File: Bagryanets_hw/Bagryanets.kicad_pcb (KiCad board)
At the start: 2 copper layers, 45 x 80 mm, 82 parts, among them Q1 SI2302CDS, Q2 SI2302CDS, Q3 SI2302CDS, U1 MCP1700-3302E_SOT23, U2 LMV721M5, U3 LMV721M5, X1 USBC-16P, X2 PLS-6 LOCK, X3 HU-2/WF-2 Battery, X4 HU-2/WF-2 SPST Switch

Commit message: Updated schematic
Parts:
- added C38: 680p, Capacitors:CAP_0603, F.Cu at (80.1, 182.1)
- added C39: 680p, Capacitors:CAP_0603, F.Cu at (80.1, 184.1)
- added C40: 100n, Capacitors:CAP_0603, F.Cu at (63.3, 125.7)
- added R15: 1k, Resistors:RES_0603, F.Cu at (76.5, 182.4)
- added R16: 1k, Resistors:RES_0603, F.Cu at (76.5, 185.2)
- C1, C10, C12, C13, C14, C16, C17, C19, C2, C21, C23, C24, C25, C3, C8: footprint Capacitors:CAP_0402 -> Capacitors:CAP_0603
- C5, C6: value * -> 1p*
- H1, H2, H3, H4: value MountingHole -> M3 MountingHole
- HA1: value HCM1201X -> HC0901A
- X3, X4: footprint Connector_PinHeader_2.54mm:PinHeader_1x02_P2.54mm_Vertical -> Connector_PinHeader_2.54mm:PinHeader_1x02_P2.54mm_Horizontal
- moved DD2 101.3 mm to (143.0, 121.0)
- moved H1 95.5 mm to (127.0, 131.0)
- moved H2 95.5 mm to (157.0, 95.0)
- moved H3 95.5 mm to (127.0, 95.0)
- moved H4 95.5 mm to (157.0, 131.0)
- moved C17 92.7 mm to (100.9, 87.2)
- moved C15 92.6 mm to (103.0, 87.2)
- moved C29 92.6 mm to (95.8, 75.3)
- moved C3 92.6 mm to (88.7, 181.2)
- moved C31 92.6 mm to (100.6, 75.6)
- moved C35 92.6 mm to (129.2, 76.8)
- moved C36 92.6 mm to (127.6, 77.3)
- moved C4 92.6 mm to (63.8, 161.9)
- moved DA1 92.6 mm to (129.7, 78.8)
- moved DD1 92.6 mm to (103.0, 82.4)
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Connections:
- C5 pad 1: /IR_IN1 -> Net-(C5-Pad1)
- C6 pad 1: /IR_IN2 -> Net-(C6-Pad1)
- DD2 pad 14: /IR_IN1 -> /L.RESET
- DD2 pad 15: /IR_IN2 -> /IR_IN1
- DD2 pad 16: /UART_TX -> /IR_IN2
- DD2 pad 17: /UART_RX -> unconnected-(DD2-PA3-Pad17)
- DD2 pad 2: unconnected-(DD2-Pad2) -> /L.DIO1
- DD2 pad 25: unconnected-(DD2-Pad25) -> /L.DIO0
- DD2 pad 26: /IR_O -> unconnected-(DD2-PB0-Pad26)
- DD2 pad 27: unconnected-(DD2-Pad27) -> /Buzzer
- DD2 pad 37: unconnected-(DD2-Pad37) -> /LED.B
- DD2 pad 38: unconnected-(DD2-Pad38) -> /LED.R
- DD2 pad 39: unconnected-(DD2-Pad39) -> /LED.G
- DD2 pad 41: /L.RESET -> /IR_Out
- DD2 pad 42: unconnected-(DD2-Pad42) -> /UART_TX
- DD2 pad 43: unconnected-(DD2-Pad43) -> /UART_RX
- DD2 pad 55: /Buzzer -> unconnected-(DD2-PB3-Pad55)
- DD2 pad 56: /LED.B -> unconnected-(DD2-PB4-Pad56)
- DD2 pad 57: /LED.R -> unconnected-(DD2-PB5-Pad57)
- DD2 pad 58: /LED.G -> unconnected-(DD2-PB6-Pad58)
- DD2 pad 7: unconnected-(DD2-Pad7) -> Net-(DD2-NRST)
- DD2 pad 8: /L.DIO0 -> unconnected-(DD2-PC0-Pad8)
- DD2 pad 9: /L.DIO1 -> unconnected-(DD2-PC1-Pad9)
- Q2 pad 1: /IR_O -> /IR_Out
- R6 pad 2: /IR_IN1 -> Net-(C5-Pad1)
- R7 pad 2: /IR_IN2 -> Net-(C6-Pad1)
- U2 pad 1: /IR_IN1 -> Net-(C5-Pad1)
- U3 pad 1: /IR_IN2 -> Net-(C6-Pad1)
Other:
- board size 45 x 80 mm -> 45 x 88 mm

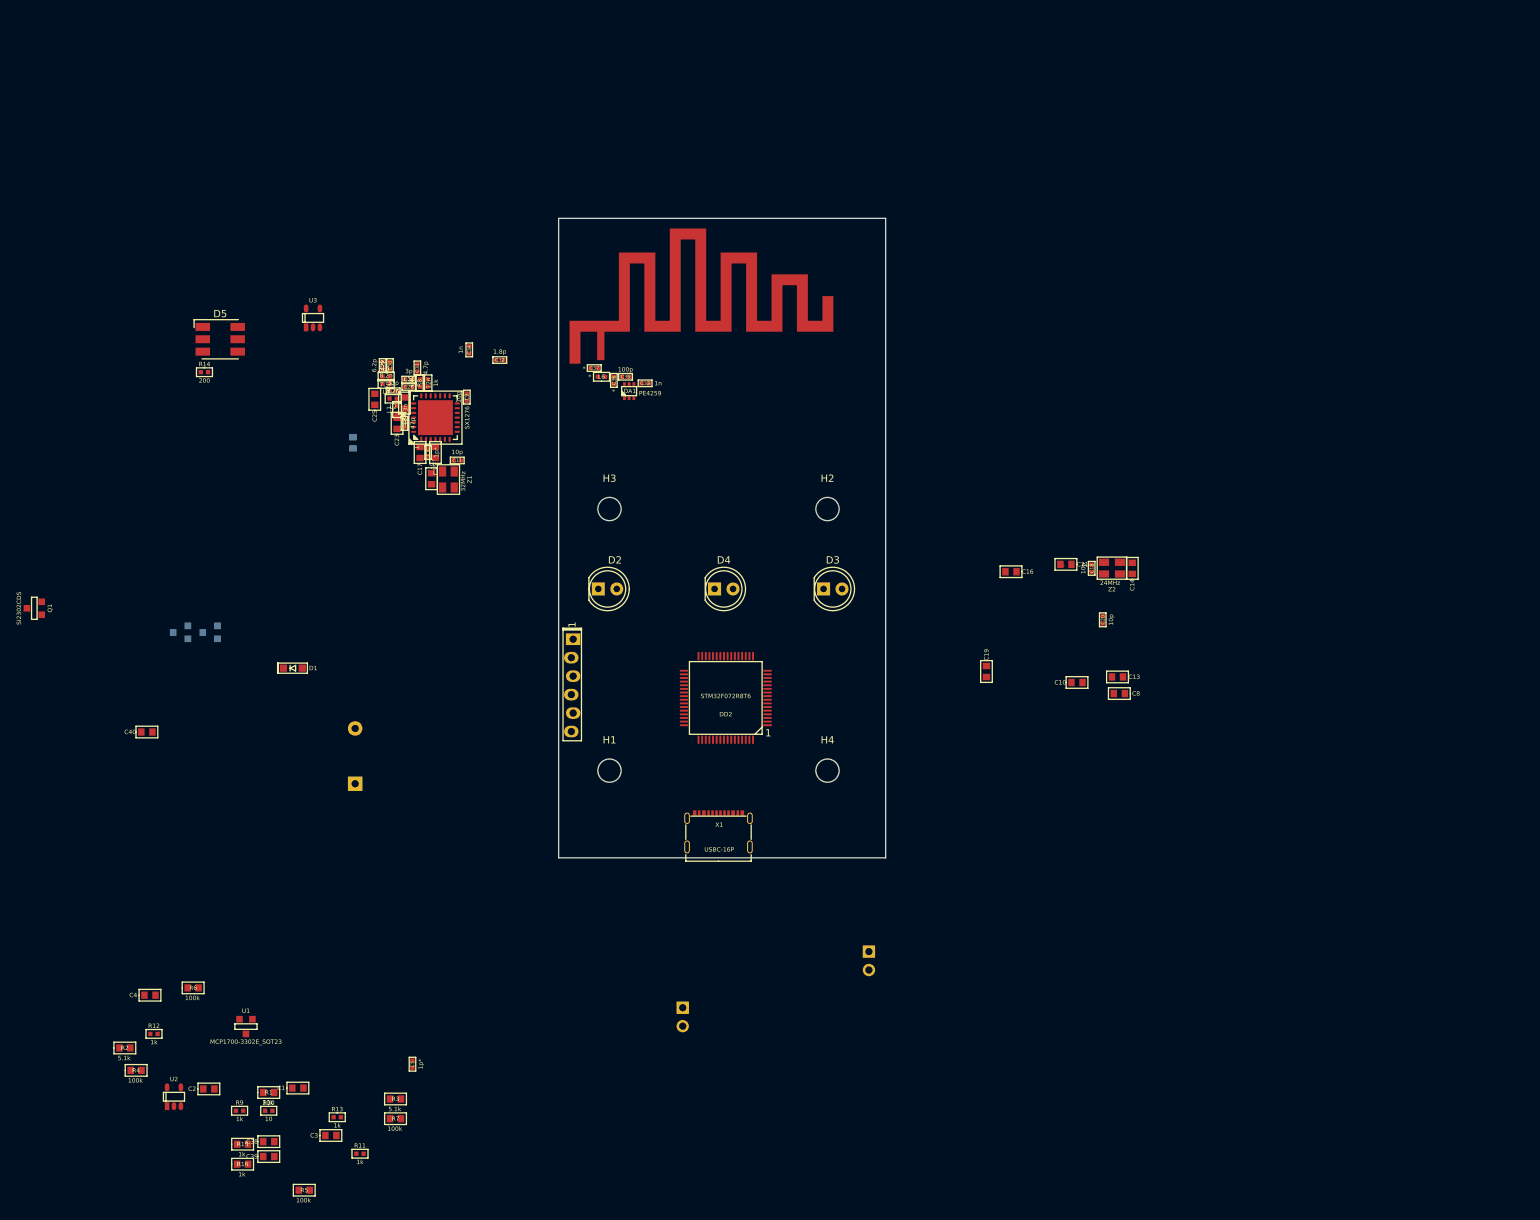
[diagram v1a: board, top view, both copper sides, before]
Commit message: PCB wiring, updated casing
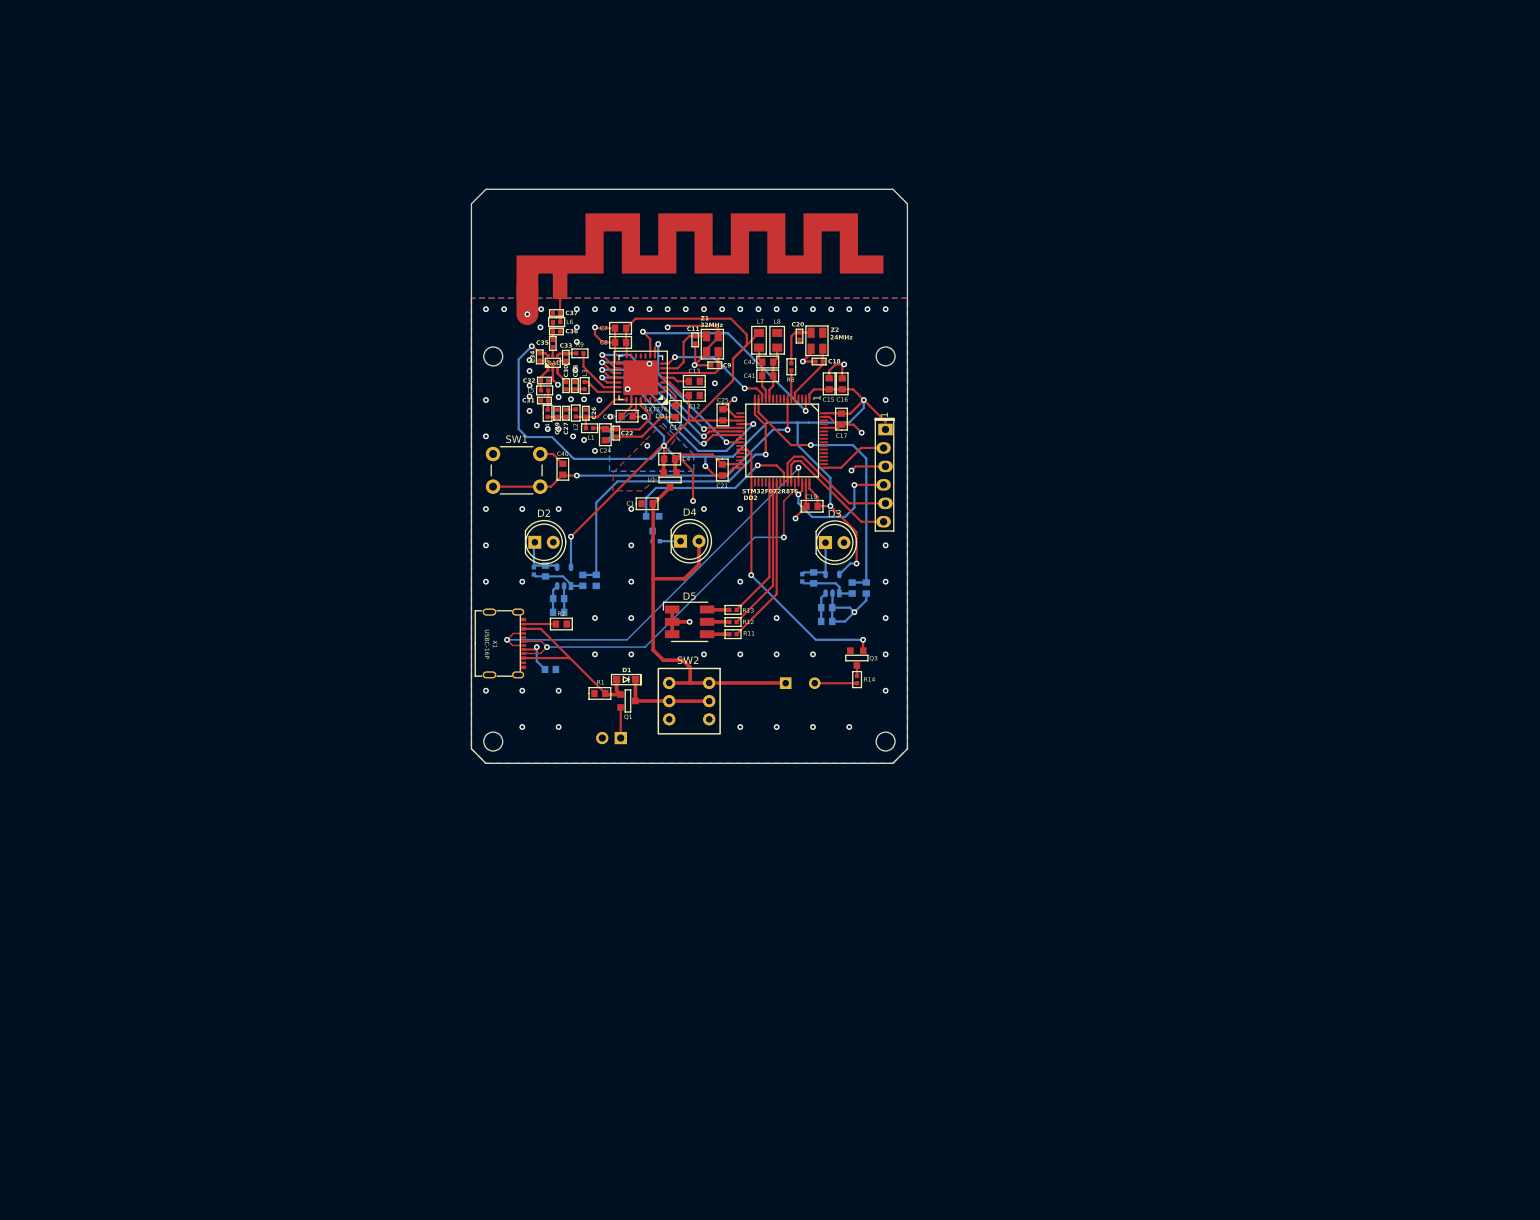
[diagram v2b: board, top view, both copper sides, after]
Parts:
- removed C23: 10n, Capacitors:CAP_0603
- removed H1, H2, H3, H4: M3 MountingHole, MountingHole:MountingHole_3.2mm_M3
- removed X4: HU-2/WF-2 SPST Switch, Connector_PinHeader_2.54mm:PinHeader_1x02_P2.54mm_Horizontal
- added ANT1: ANT_GENERAL, Kais_Lib:Antenna_868_Bagryanets, F.Cu at (120.2, 66.1)
- added C41: 10n, Capacitors:CAP_0603, F.Cu at (148.8, 76.7)
- added C42: 10u, Capacitors:CAP_0603, F.Cu at (148.8, 74.8)
- added L7: 10uH, Inductors:IND_0805, F.Cu at (147.6, 71.8)
- added L8: 10uH, Inductors:IND_0805, F.Cu at (150.1, 71.8)
- added SW1: SW_Push, BtnsSwitches:SW_PUSH_6mm, F.Cu at (111.0, 87.4)
- added SW2: KLS7-P8.5x8.5, Kais_Lib:KLS7-P8.5x8.5, F.Cu at (144.7, 120.9)
- C12, Q3: moved to F.Cu
- C2, C3, C38, C39, C5, C6, R10, R15, R16, R3, R4, R5, R6, R7, U2, U3: moved to B.Cu
- HA1: footprint Buzzer_Beeper:Buzzer_12x9.5RM7.6 -> Buzzer_Beeper:MagneticBuzzer_CUI_CST-931RP-A
- moved R16 115.4 mm to (160.4, 105.9), turned to 90 degrees
- moved R9 114.3 mm to (122.9, 73.6), turned to 180 degrees
- moved C39 113.5 mm to (162.3, 105.9), turned to -90 degrees
- moved R5 107.7 mm to (156.9, 108.6)
- moved C4 102.8 mm to (135.3, 88.1), turned to 180 degrees
- moved R14 99.3 mm to (161.1, 118.5), turned to -90 degrees
- moved C3 98.3 mm to (156.9, 110.5), turned to 180 degrees
- moved R12 97.8 mm to (144.0, 110.5)
- moved U1 95.2 mm to (135.3, 91.0)
- moved R10 94.8 mm to (133.4, 99.4), turned to 180 degrees
- moved R7 94.1 mm to (155.1, 104.5), turned to -90 degrees
- moved C1 93.7 mm to (132.2, 94.3)
- moved R15 90.6 mm to (123.3, 104.8), turned to 90 degrees
- moved U2 89.5 mm to (120.8, 104.3), turned to 180 degrees
- moved C38 89.4 mm to (125.2, 104.8), turned to -90 degrees
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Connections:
- net /L.OSK_IN renamed /L.OSC_IN
- net /L.OSK_OUT renamed /L.OSC_OUT
- net /OSK_IN renamed /OSC_IN
- net /OSK_OUT renamed /OSC_OUT
- D5 pad 1: Net-(D5-RK) -> GND
- D5 pad 2: Net-(D5-GK) -> GND
- D5 pad 3: Net-(D5-BK) -> GND
- D5 pad 4: GND -> Net-(D5-BA)
- D5 pad 5: GND -> Net-(D5-GA)
- D5 pad 6: GND -> Net-(D5-RA)
- DD2 pad 12: GND -> /VSSA
- DD2 pad 13: +3V3 -> /VDDA
- DD2 pad 15: /IR_IN1 -> /IR_IN2
- DD2 pad 16: /IR_IN2 -> /IR_IN1
- R11 pad 1: Net-(D5-RK) -> Net-(D5-BA)
- R11 pad 2: /LED.B -> /LED.G
- R12 pad 1: Net-(D5-GK) -> Net-(D5-GA)
- R13 pad 1: Net-(D5-BK) -> Net-(D5-RA)
- R13 pad 2: /LED.G -> /LED.B
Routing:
- net +3V3: track 0.27 -> 225.1 mm, vias 0 -> 9
- net GND: track 0.00 -> 146.1 mm, vias 0 -> 96
- net /Unst.power: track 0.00 -> 58.1 mm
- net /USB.D+: track 0.00 -> 57.1 mm, vias 0 -> 2
- net /USB.D-: track 0.00 -> 54.3 mm, vias 0 -> 2
- net Net-(DD2-NRST): track 0.00 -> 48.1 mm, vias 0 -> 2
- net /IR_IN1: track 0.00 -> 46.2 mm, vias 0 -> 1
- net /Buzzer: track 0.00 -> 39.0 mm, vias 0 -> 2
- net /IR_IN2: track 0.00 -> 38.4 mm, vias 0 -> 1
- net /L.DIO1: track 0.00 -> 32.4 mm, vias 0 -> 2
- net /L.NSS: track 0.00 -> 30.9 mm, vias 0 -> 2
- net /L.MOSI: track 0.00 -> 26.5 mm, vias 0 -> 2
- net /L.MISO: track 0.00 -> 26.5 mm, vias 0 -> 2
- net /L.SCK: track 0.00 -> 26.4 mm, vias 0 -> 2
- net /USB.power: track 0.00 -> 25.8 mm
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- added copper zone on B.Cu, net +3V3
- added copper zone on F.Cu, net +3V3
- added copper zone on B.Cu, net GND
- added copper zone on F.Cu, net GND
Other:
- board size 45 x 88 mm -> 60 x 79 mm

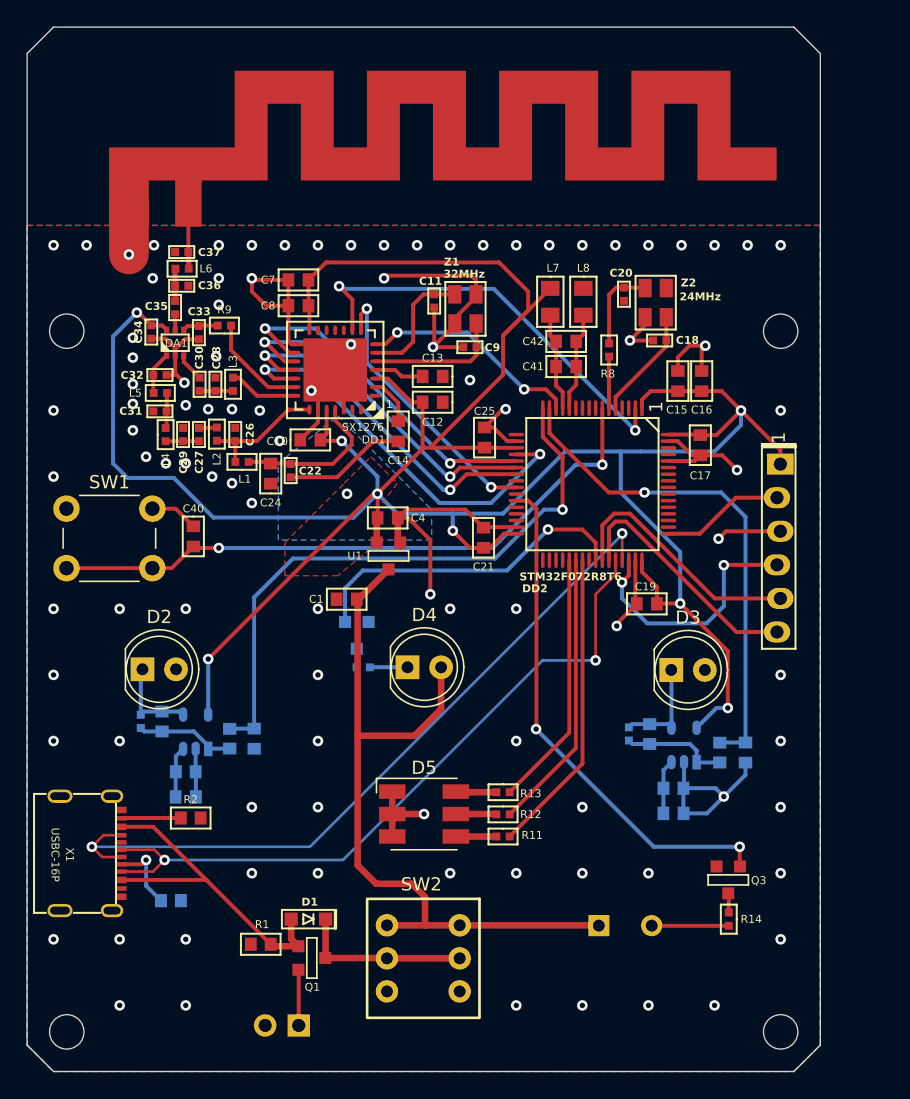
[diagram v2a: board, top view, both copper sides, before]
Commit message: Added LSE clock, USB protection, battery monitoring to schematic, PCB rewiring, cover update
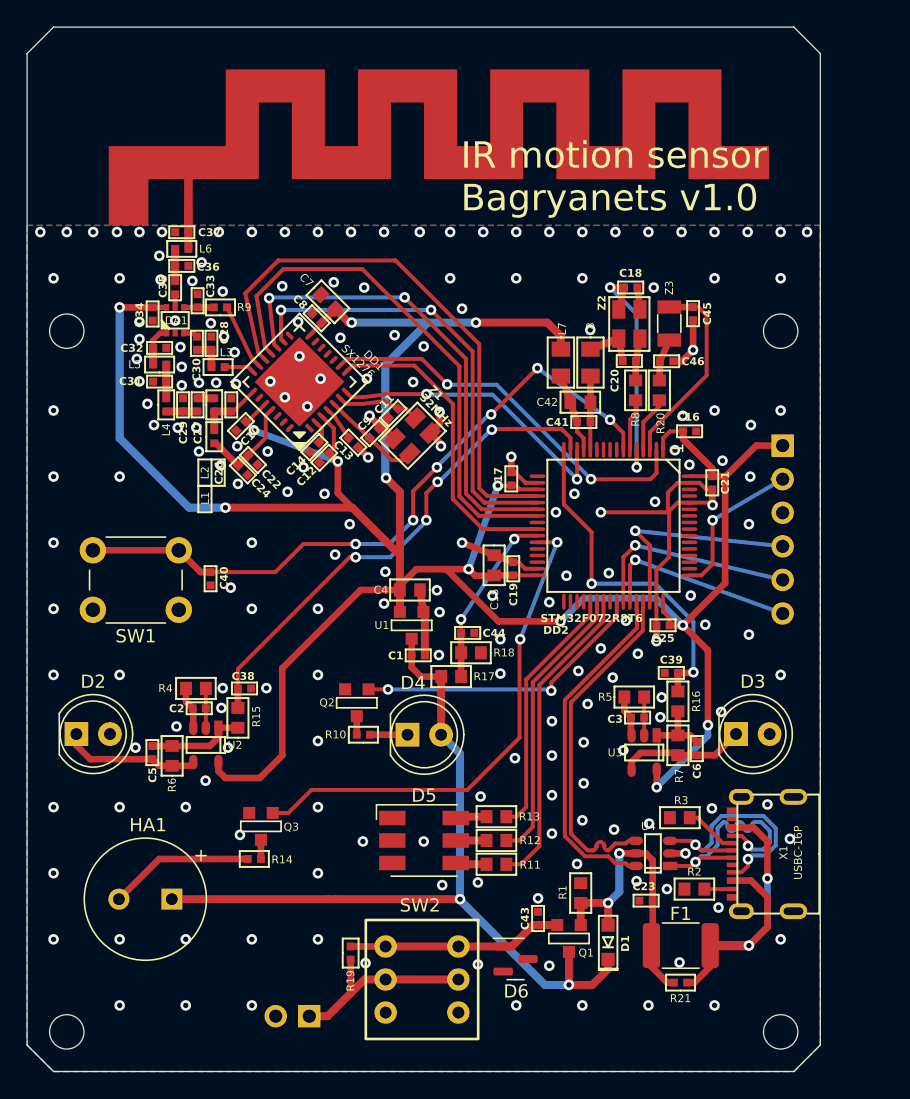
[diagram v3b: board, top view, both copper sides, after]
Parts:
- added C23: 100n, Capacitors:CAP_0402, F.Cu at (154.8, 117.1)
- added C43: 100n, Capacitors:CAP_0402, F.Cu at (146.7, 118.4)
- added C44: 100n, Capacitors:CAP_0402, F.Cu at (141.3, 96.8)
- added C45: 12.5p, Capacitors:CAP_0402, F.Cu at (158.4, 72.7)
- added C46: 12.5p, Capacitors:CAP_0402, F.Cu at (156.4, 76.3)
- added D6: ESDA5V3L, Package_TO_SOT_SMD:SOT-23, F.Cu at (144.9, 121.5)
- added F1: MF-MSMF050, Fuse:Fuse_1812_4532Metric_Pad1.30x3.40mm_HandSolder, F.Cu at (157.4, 120.5)
- added G***: LOGO, LOGO, B.Cu at (117.1, 58.8)
- added R17: 100k, Resistors:RES_0603, F.Cu at (140.1, 100.1)
- added R18: 100k, Resistors:RES_0603, F.Cu at (141.6, 98.3)
- added R19: *, Resistors:RES_0402, F.Cu at (132.5, 121.0)
- added R20: 100k, Resistors:RES_0603, F.Cu at (155.8, 78.5)
- added R21: *, Resistors:RES_0402, F.Cu at (157.4, 123.3)
- added U4: USBLC6_2SC6, SOT:SOT23-6, F.Cu at (155.3, 113.5)
- added Z3: 32.768kHz, Crystal:Crystal_SMD_3215-2Pin_3.2x1.5mm, F.Cu at (156.6, 73.4)
- C1, C10, C12, C13, C14, C16, C17, C19, C21, C24, C25, C40, C41, C8: footprint Capacitors:CAP_0603 -> Capacitors:CAP_0402
- C2, C3, C38, C39: footprint Capacitors:CAP_0603 -> Capacitors:CAP_0402; moved to F.Cu
- C5, C6, Q2, R10, R15, R16, R3, R4, R5, R6, R7, U2, U3: moved to F.Cu
- HA1: value HC0901A -> HC0903A; moved to F.Cu
- R11, R12, R13, R8: footprint Resistors:RES_0402 -> Resistors:RES_0603
- X2: footprint Connectors:PLS-6_LOCK -> Connector_PinHeader_2.54mm:PinHeader_1x06_P2.54mm_Horizontal
- moved X1 47.6 mm to (162.0, 113.5), turned to 90 degrees
- moved R3 39.0 mm to (157.4, 110.8), turned to 180 degrees
- moved R2 38.5 mm to (158.5, 116.2), turned to 180 degrees
- moved R14 36.2 mm to (125.2, 113.9), turned to 180 degrees
- moved Q3 35.6 mm to (125.7, 111.5)
- moved HA1 32.4 mm to (118.9, 117.0)
- moved R1 24.5 mm to (149.9, 116.5), turned to -90 degrees
- moved D1 22.7 mm to (151.9, 120.2), turned to 90 degrees
- moved C15 19.7 mm to (143.3, 91.7)
- moved C25 19.6 mm to (156.1, 96.2), turned to 0 degrees
- moved Q1 19.5 mm to (149.0, 119.9), turned to 0 degrees
- moved C21 17.8 mm to (159.8, 85.5), turned to 90 degrees
- moved C17 14.5 mm to (144.6, 85.2), turned to -90 degrees
- moved SW1 11.4 mm to (119.5, 95.1), turned to 180 degrees
- moved C19 10.4 mm to (144.8, 92.0), turned to -90 degrees
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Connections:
- D1 pad C: Net-(Q1-D) -> /Unst.power
- DD2 pad 15: /IR_IN2 -> /IR_IN1
- DD2 pad 16: /IR_IN1 -> /IR_IN2
- DD2 pad 26: unconnected-(DD2-PB0-Pad26) -> /BatCtrl
- DD2 pad 3: unconnected-(DD2-PC14-Pad3) -> /OSC32_IN
- DD2 pad 4: unconnected-(DD2-PC15-Pad4) -> /OSC32_OUT
- Q1 pad 3: Net-(Q1-D) -> /Unst.power
- SW2 pad 1: /Unst.power -> /Battery
- SW2 pad 2: Net-(Q1-D) -> Net-(R19-Pad1)
- SW2 pad 4: /Unst.power -> /Battery
- SW2 pad 5: Net-(Q1-D) -> Net-(R19-Pad1)
- X1 pad A4B9: /USB.power -> /VBUS
- X1 pad A6: /USB.D+ -> /Conn.D+
- X1 pad A7: /USB.D- -> /Conn.D-
- X1 pad B4A9: /USB.power -> /VBUS
- X1 pad B6: /USB.D+ -> /Conn.D+
- X1 pad B7: /USB.D- -> /Conn.D-
- X3 pad 1: /Battery -> Net-(R19-Pad1)
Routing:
- net GND: track 146.1 -> 65.5 mm, vias 96 -> 197
- net /USB.D+: track 57.1 -> 26.2 mm, vias 2 -> 0
- net /USB.D-: track 54.3 -> 26.3 mm, vias 2 -> 0
- net /VBUS: track 0.00 -> 25.8 mm, vias 0 -> 2
- net /Conn.D+: track 0.00 -> 19.2 mm, vias 0 -> 2
- net /Conn.D-: track 0.00 -> 19.0 mm, vias 0 -> 2
- net /OSC32_IN: track 0.00 -> 15.0 mm
- net Net-(R19-Pad1): track 0.00 -> 15.0 mm
- net /L.MOSI: track 26.5 -> 40.2 mm, vias 2 -> 0
- net /BatCtrl: track 0.00 -> 13.5 mm, vias 0 -> 2
- net Net-(Q1-D): track 13.1 -> 0.00 mm
- net /IR_IN2: track 38.4 -> 26.3 mm, vias 1 -> 2
- net /Battery: track 4.22 -> 16.3 mm
- net /L.NSS: track 30.9 -> 42.2 mm, vias 2 -> 0
- net /L.MISO: track 26.5 -> 36.8 mm
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- removed copper zone on B.Cu, net +3V3
- removed copper zone on F.Cu, net +3V3
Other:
- board text added: "IR motion sensor Bagryanets v1.0"

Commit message: Minor PCB changes
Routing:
- net GND: track 65.5 -> 70.0 mm, vias 197 -> 195
- net /Buzzer: track 37.8 -> 37.3 mm

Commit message: GOST designators
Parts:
- R14: renamed from R20; value 100k -> 1k
- renumbered C44 to C1, C6 to C10, C5 to C11, C9 to C12, C10 to C13, C11 to C14, C39 to C15, C38 to C16, C12 to C17, C45 to C18, C18 to C19, C23 to C2, C13 to C20, C15 to C21, C14 to C22, C46 to C23, C20 to C24, C16 to C25, C17 to C26, C42 to C27, C19 to C28, C41 to C29, C1 to C3, C21 to C30, C40 to C31, C25 to C32, C22 to C33, C24 to C34, C26 to C35, C27 to C36, C28 to C37, C29 to C38, C30 to C39, C43 to C4, C31 to C40, C32 to C41, C33 to C42, C34 to C43, C35 to C44, C36 to C45, C37 to C46, C4 to C5, C3 to C6, C2 to C7, C7 to C8, C8 to C9, U1 to DA1, U3 to DA2, U2 to DA3, DA1 to DA4, DD2 to DD1, L7 to L1, L8 to L2, L1 to L3, L2 to L4, L3 to L5, L4 to L6, L5 to L7, L6 to L8, R7 to R10, R6 to R11, R16 to R12, R15 to R13, R8 to R15, R9 to R16, R10 to R17, R11 to R18, R12 to R19, R17 to R2, R13 to R20, R14 to R21, R18 to R3, R2 to R4, R3 to R5, R21 to R6, R19 to R7, R5 to R8, R4 to R9, SW2 to SB1, SW1 to SB2, DD1 to U1, D1 to VD1, U4 to VD2, D6 to VD3, D3 to VD4, D2 to VD5, D4 to VD6, D5 to VD7, Q1 to VT1, Q2 to VT2, Q3 to VT3, ANT1 to WA1, X2 to XP1, X3 to XP2, X1 to XS1, Z1 to ZQ1, Z3 to ZQ2, Z2 to ZQ3

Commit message: Added STL
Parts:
- added H1: MountingHole, Kais_Lib:Hole_2.4, F.Cu at (111.0, 74.0)
- added H2: MountingHole, Kais_Lib:Hole_2.4, F.Cu at (165.0, 74.0)
- added H3: MountingHole, Kais_Lib:Hole_2.4, F.Cu at (111.0, 127.0)
- added H4: MountingHole, Kais_Lib:Hole_2.4, F.Cu at (165.0, 127.0)
- added R22: *, Resistors:RES_0603, F.Cu at (122.3, 90.0)
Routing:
- net GND: track 70.0 -> 73.9 mm, vias 195 -> 194
- net +3V3: track 214.8 -> 217.0 mm
- net Net-(DD1-NRST): track 51.4 -> 53.1 mm
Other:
- outline, holes or cut-outs redrawn
